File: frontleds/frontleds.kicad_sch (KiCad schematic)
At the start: 1 part, among them J1 Conn_01x02_MountingPin

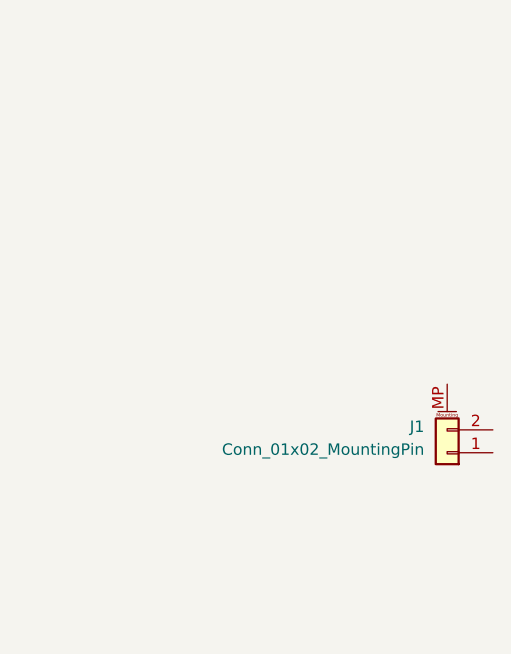
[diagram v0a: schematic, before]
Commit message: front led base layout done, should probably move resistors onto this board
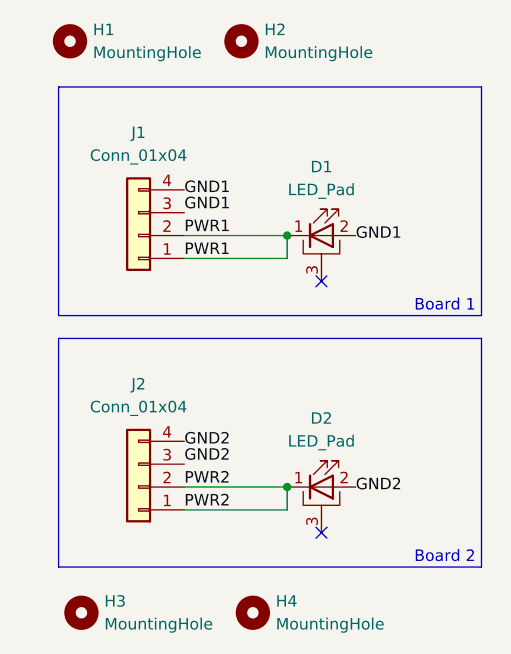
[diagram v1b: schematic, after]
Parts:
- removed J1: Conn_01x02_MountingPin, Connector_JST:JST_PH_B2B-PH-SM4-TB_1x02-1MP_P2.00mm_Vertical, symbol Connector_Generic_MountingPin:Conn_01x02_MountingPin
- added D1, D2: LED_Pad, LED_SMD:LED_Cree-XP-GWT, symbol Device:LED_Pad
- added H1, H2, H3, H4: MountingHole, MountingHole:MountingHole_2.7mm_M2.5_DIN965, symbol Mechanical:MountingHole
- added J1, J2: Conn_01x04, Connector_JST:JST_PH_B4B-PH-K_1x04_P2.00mm_Vertical, symbol Connector_Generic:Conn_01x04
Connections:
- new net GND1: D1.2 (A), J1.3 (Pin_3), J1.4 (Pin_4)
- new net GND2: D2.2 (A), J2.3 (Pin_3), J2.4 (Pin_4)
- new net PWR1: D1.1 (K), J1.1 (Pin_1), J1.2 (Pin_2)
- new net PWR2: D2.1 (K), J2.1 (Pin_1), J2.2 (Pin_2)
- no-connect marks 0 -> 2
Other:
- note added: "Board 1"
- note added: "Board 2"

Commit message: smol boi
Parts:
- removed D2: LED_Pad, LED_SMD:LED_Cree-XP-GWT, symbol Device:LED_Pad
- removed H1, H2, H3, H4: MountingHole, MountingHole:MountingHole_2.7mm_M2.5_DIN965, symbol Mechanical:MountingHole
- removed J1, J2: Conn_01x04, Connector_JST:JST_PH_B4B-PH-K_1x04_P2.00mm_Vertical, symbol Connector_Generic:Conn_01x04
- added J3: Conn_02x10_Odd_Even, Connector_Samtec_HSEC8:Samtec_HSEC8-110-X-X-DV_2x10_P0.8mm_Edge, symbol Connector_Generic:Conn_02x10_Odd_Even
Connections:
- net GND1 is gone; now on net PWR1: D1.2 (A)
- net PWR1: now also J3.10 (Pin_10), J3.12 (Pin_12), J3.14 (Pin_14), J3.16 (Pin_16), J3.18 (Pin_18), J3.2 (Pin_2), J3.20 (Pin_20), J3.4 (Pin_4), J3.6 (Pin_6), J3.8 (Pin_8); no longer D1.1 (K)
- new net GND: D1.1 (K), J3.1 (Pin_1), J3.11 (Pin_11), J3.13 (Pin_13), J3.15 (Pin_15), J3.17 (Pin_17), J3.19 (Pin_19), J3.3 (Pin_3), J3.5 (Pin_5), J3.7 (Pin_7), J3.9 (Pin_9)
- no-connect marks 2 -> 1
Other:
- note removed: "Board 1"
- note removed: "Board 2"
- moved on the sheet: D1

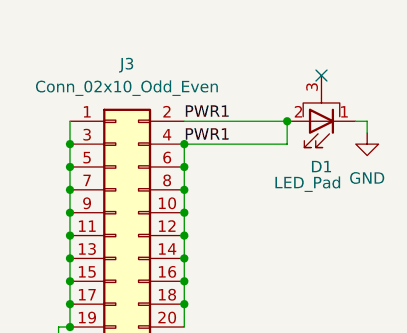
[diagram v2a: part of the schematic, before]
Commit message: changed front leds to use dedicated led current drivers
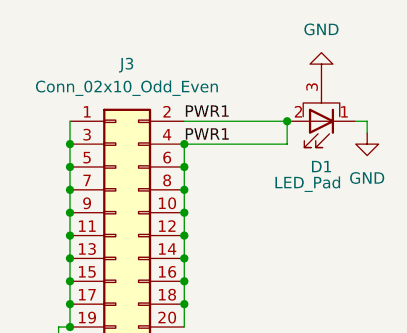
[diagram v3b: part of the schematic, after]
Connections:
- net GND: now also D1.3 (PAD)
- no-connect marks 1 -> 0
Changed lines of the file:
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@@
 		(color 0 0 0 0)
-	)
-	(no_connect
-		(at 69.85 54.61)
 	)
 	(wire
@@
 					(unit 1)
 				)
+			)
+		)
+	)
+	(symbol
+		(lib_id "power:GND")
+		(at 69.85 54.61 180)
+		(unit 1)
+		(exclude_from_sim no)
+		(in_bom yes)
+		(on_board yes)
+		(dnp no)
+		(fields_autoplaced yes)
+		(property "Reference" "#PWR03"
+			(at 69.85 48.26 0)
+			(effects
+				(font
+					(size 1.27 1.27)
+				)
+				(hide yes)
+			)
+		)
+		(property "Value" "GND"
+			(at 69.85 49.53 0)
+			(effects
+				(font
+					(size 1.27 1.27)
+				)
+			)
+		)
+		(property "Footprint" ""
+			(at 69.85 54.61 0)
+			(effects
+				(font
+					(size 1.27 1.27)
+				)
+				(hide yes)
+			)
+		)
+		(property "Datasheet" ""
+			(at 69.85 54.61 0)
+			(effects
+				(font
+					(size 1.27 1.27)
+				)
+				(hide yes)
+			)
+		)
+		(property "Description" "Power symbol creates a global label with name \"GND\" , ground"
+			(at 69.85 54.61 0)
+			(effects
+				(font
+					(size 1.27 1.27)
+				)
+				(hide yes)
+			)
+		)
+		(pin "1"
+		)
+		(instances
+			(project "frontleds"
+				(path "/ad2684eb-c2bb-4fca-b716-3281952c7862"
+					(reference "#PWR03")
+					(unit 1)
+				)

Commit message: small changes to leds
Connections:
- net PWR1 renamed PWR
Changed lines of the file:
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@@
-	)
-	(junction
-		(at 66.04 59.69)
-		(diameter 0)
-		(color 0 0 0 0)
 	)
 	(junction
@@
 	)
 	(junction
+		(at 54.61 59.69)
+		(diameter 0)
+		(color 0 0 0 0)
+	)
+	(junction
 		(at 54.61 77.47)
 		(diameter 0)
@@
 	)
 	(junction
+		(at 54.61 67.31)
+		(diameter 0)
+		(color 0 0 0 0)
+	)
+	(junction
+		(at 41.91 82.55)
+		(diameter 0)
+		(color 0 0 0 0)
+	)
+	(junction
 		(at 54.61 62.23)
 		(diameter 0)
@@
 	)
 	(junction
-		(at 54.61 67.31)
-		(diameter 0)
-		(color 0 0 0 0)
-	)
-	(junction
-		(at 41.91 82.55)
-		(diameter 0)
-		(color 0 0 0 0)
-	)
-	(junction
 		(at 41.91 77.47)
 		(diameter 0)
@@
 	(wire
 		(pts
+			(xy 54.61 59.69) (xy 54.61 62.23)
+		)
+		(stroke
+			(width 0)
+			(type default)
+		)
+	)
+	(wire
+		(pts
 			(xy 74.93 60.96) (xy 74.93 59.69)
 		)
@@
 	(wire
 		(pts
-			(xy 66.04 62.23) (xy 66.04 59.69)
-		)
-		(stroke
-			(width 0)
-			(type default)
-		)
-	)
-	(wire
-		(pts
 			(xy 41.91 77.47) (xy 41.91 80.01)
 		)
@@
 	(wire
 		(pts
-			(xy 54.61 62.23) (xy 66.04 62.23)
-		)
-		(stroke
-			(width 0)
-			(type default)
-		)
-	)
-	(wire
-		(pts
 			(xy 54.61 67.31) (xy 54.61 69.85)
 		)
@@
 		)
 	)
-	(label "PWR1"
+	(label "PWR"
 		(at 54.61 59.69 0)
 		(effects
 			(font
-				(size 1.27 1.27)
-			)
-			(justify left bottom)
-		)
-	)
-	(label "PWR1"
-		(at 54.61 62.23 0)
-		(effects
-			(font

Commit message: Production of leds and pcb
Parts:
- D1: LCSC (none) -> C17401863
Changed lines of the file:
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@@
+			)
+		)
+		(property "LCSC" "C17401863"
+			(at 69.85 59.69 0)
+			(effects
+				(font
+					(size 1.27 1.27)
+				)
+				(hide yes)
 			)
 		)

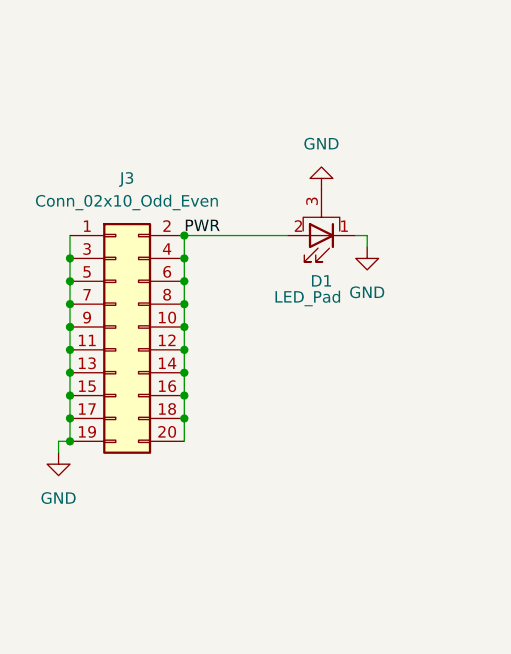
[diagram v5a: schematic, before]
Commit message: bro how does this work (fix led symbol footprint and model)
idk why frontleds can use drylettuce symbols but not footprints/3d models liek whaaaaa
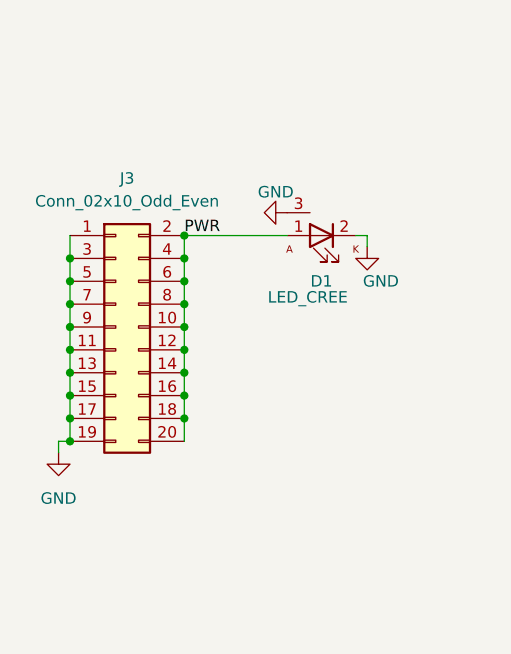
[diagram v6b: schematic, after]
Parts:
- D1: value LED_Pad -> LED_CREE; footprint LED_SMD:LED_Cree-XP-GWT -> Dry_Lettuce_LED:LED_Cree-XPGBWT; symbol Device:LED_Pad -> Dry_Lettuce:LED_CREE-XPGBWT
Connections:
- net GND: now also D1.2 (A); no longer D1.1 (K)
- net PWR: now also D1.1 (K); no longer D1.2 (A)
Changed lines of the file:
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@@
 (kicad_sch
-	(version 20250114)
+	(version 20260306)
 	(generator "eeschema")
-	(generator_version "9.0")
+	(generator_version "10.0")
 	(paper "A4")
 	(junction
@@
 		(at 46.99 69.85 0)
 		(unit 1)
+		(body_style 1)
 		(exclude_from_sim no)
 		(in_bom yes)
 		(on_board yes)
+		(in_pos_files yes)
 		(dnp no)
 		(fields_autoplaced yes)
 		(property "Reference" "J3"
 			(at 48.26 53.34 0)
+			(show_name no)
+			(do_not_autoplace no)
 			(effects
 				(font
@@
 		(property "Value" "Conn_02x10_Odd_Even"
 			(at 48.26 55.88 0)
+			(show_name no)
+			(do_not_autoplace no)
 			(effects
 				(font
@@
 		(property "Footprint" "Connector_Samtec_HSEC8:Samtec_HSEC8-110-X-X-DV_2x10_P0.8mm_Edge"
 			(at 46.99 69.85 0)
-			(effects
-				(font
-					(size 1.27 1.27)
-				)
-				(hide yes)
-			)
-		)
-		(property "Datasheet" "~"
+			(hide yes)
+			(show_name no)
+			(do_not_autoplace no)
+			(effects
+				(font
+					(size 1.27 1.27)
+				)
+			)
+		)
+		(property "Datasheet" ""
 			(at 46.99 69.85 0)
-			(effects
-				(font
-					(size 1.27 1.27)
-				)
-				(hide yes)
+			(hide yes)
+			(show_name no)
+			(do_not_autoplace no)
+			(effects
+				(font
+					(size 1.27 1.27)
+				)
 			)
 		)
 		(property "Description" "Generic connector, double row, 02x10, odd/even pin numbering scheme (row 1 odd numbers, row 2 even numbers), script generated (kicad-library-utils/schlib/autogen/connector/)"
 			(at 46.99 69.85 0)
-			(effects
-				(font
-					(size 1.27 1.27)
-				)
-				(hide yes)
+			(hide yes)
+			(show_name no)
+			(do_not_autoplace no)
+			(effects
+				(font
+					(size 1.27 1.27)
+				)
 			)
 		)
@@
 		)
 		(instances
-			(project ""
+			(project "frontleds"
 				(path "/ad2684eb-c2bb-4fca-b716-3281952c7862"
 					(reference "J3")
@@
 	(symbol
 		(lib_id "power:GND")
-		(at 69.85 54.61 180)
+		(at 66.04 57.15 270)
 		(unit 1)
+		(body_style 1)
 		(exclude_from_sim no)
 		(in_bom yes)
 		(on_board yes)
+		(in_pos_files yes)
 		(dnp no)
-		(fields_autoplaced yes)
 		(property "Reference" "#PWR03"
-			(at 69.85 48.26 0)
-			(effects
-				(font
-					(size 1.27 1.27)
-				)
-				(hide yes)
+			(at 59.69 57.15 0)
+			(hide yes)
+			(show_name no)
+			(do_not_autoplace no)
+			(effects
+				(font
+					(size 1.27 1.27)
+				)
 			)
 		)
 		(property "Value" "GND"
-			(at 69.85 49.53 0)
+			(at 64.77 54.864 90)
+			(show_name no)
+			(do_not_autoplace no)
 			(effects
 				(font
@@
 		)
 		(property "Footprint" ""
-			(at 69.85 54.61 0)
-			(effects
-				(font
-					(size 1.27 1.27)
-				)
-				(hide yes)
+			(at 66.04 57.15 0)
+			(hide yes)
+			(show_name no)
+			(do_not_autoplace no)
+			(effects
+				(font
+					(size 1.27 1.27)
+				)
 			)
 		)
 		(property "Datasheet" ""
-			(at 69.85 54.61 0)
-			(effects
-				(font
-					(size 1.27 1.27)
-				)
-				(hide yes)
+			(at 66.04 57.15 0)
+			(hide yes)
+			(show_name no)
+			(do_not_autoplace no)
+			(effects
+				(font
+					(size 1.27 1.27)
+				)
 			)
 		)
 		(property "Description" "Power symbol creates a global label with name \"GND\" , ground"
-			(at 69.85 54.61 0)
-			(effects
-				(font
-					(size 1.27 1.27)
-				)
-				(hide yes)
+			(at 66.04 57.15 0)
+			(hide yes)
+			(show_name no)
+			(do_not_autoplace no)
+			(effects
+				(font
+					(size 1.27 1.27)
+				)
 			)
 		)
@@
 	)
 	(symbol
-		(lib_id "Device:LED_Pad")
+		(lib_id "Dry_Lettuce:LED_CREE-XPGBWT")
 		(at 69.85 59.69 180)
 		(unit 1)
+		(body_style 1)
 		(exclude_from_sim no)
 		(in_bom yes)
 		(on_board yes)
+		(in_pos_files yes)
 		(dnp no)
 		(property "Reference" "D1"
 			(at 69.85 64.77 0)
-			(effects
-				(font
-					(size 1.27 1.27)
-				)
-			)
-		)
-		(property "Value" "LED_Pad"
+			(show_name no)
+			(do_not_autoplace no)
+			(effects
+				(font
+					(size 1.27 1.27)
+				)
+			)
+		)
+		(property "Value" "LED_CREE"
 			(at 68.326 66.548 0)
-			(effects
-				(font
-					(size 1.27 1.27)
-				)
-			)
-		)
-		(property "Footprint" "LED_SMD:LED_Cree-XP-GWT"
+			(show_name no)
+			(do_not_autoplace no)
+			(effects
+				(font
+					(size 1.27 1.27)
+				)
+			)
+		)
+		(property "Footprint" "Dry_Lettuce_LED:LED_Cree-XPGBWT"
 			(at 69.85 59.69 0)
-			(effects
-				(font
-					(size 1.27 1.27)
-				)
-				(hide yes)
-			)
-		)
-		(property "Datasheet" "~"
+			(hide yes)
+			(show_name no)
+			(do_not_autoplace no)
+			(effects
+				(font
+					(size 1.27 1.27)
+				)
+			)
+		)
+		(property "Datasheet" ""
 			(at 69.85 59.69 0)
-			(effects
-				(font
-					(size 1.27 1.27)
-				)
-				(hide yes)
+			(hide yes)
+			(show_name no)
+			(do_not_autoplace no)
+			(effects
+				(font
+					(size 1.27 1.27)
+				)
 			)
 		)
 		(property "Description" "Light emitting diode with pad"
-			(at 69.85 59.69 0)
-			(effects
-				(font
-					(size 1.27 1.27)
-				)
-				(hide yes)
+			(at 70.358 52.07 0)
+			(hide yes)
+			(show_name no)
+			(do_not_autoplace no)
+			(effects
+				(font
+					(size 1.27 1.27)
+				)
 			)
 		)
 		(property "LCSC" "C17401863"
 			(at 69.85 59.69 0)
-			(effects
-				(font
-					(size 1.27 1.27)
-				)
-				(hide yes)
+			(hide yes)
+			(show_name no)
+			(do_not_autoplace no)
+			(effects
+				(font
+					(size 1.27 1.27)
+				)
 			)
 		)
@@
 		)
 		(instances
-			(project ""
+			(project "frontleds"
 				(path "/ad2684eb-c2bb-4fca-b716-3281952c7862"
 					(reference "D1")
@@
 		(at 40.64 83.82 0)
 		(unit 1)
+		(body_style 1)
 		(exclude_from_sim no)
 		(in_bom yes)
 		(on_board yes)
+		(in_pos_files yes)
 		(dnp no)
 		(fields_autoplaced yes)
 		(property "Reference" "#PWR02"
 			(at 40.64 90.17 0)
-			(effects
-				(font
-					(size 1.27 1.27)
-				)
-				(hide yes)
+			(hide yes)
+			(show_name no)
+			(do_not_autoplace no)
+			(effects
+				(font
+					(size 1.27 1.27)
+				)
 			)
 		)
 		(property "Value" "GND"
 			(at 40.64 88.9 0)
+			(show_name no)
+			(do_not_autoplace no)
 			(effects
 				(font
@@
 		(property "Footprint" ""
 			(at 40.64 83.82 0)
-			(effects
-				(font
-					(size 1.27 1.27)
-				)
-				(hide yes)
+			(hide yes)
+			(show_name no)
+			(do_not_autoplace no)
+			(effects
+				(font
+					(size 1.27 1.27)
+				)
 			)
 		)
 		(property "Datasheet" ""
 			(at 40.64 83.82 0)
-			(effects
-				(font
-					(size 1.27 1.27)
-				)
-				(hide yes)
+			(hide yes)
+			(show_name no)
+			(do_not_autoplace no)
+			(effects
+				(font
+					(size 1.27 1.27)
+				)
 			)
 		)
 		(property "Description" "Power symbol creates a global label with name \"GND\" , ground"
 			(at 40.64 83.82 0)
-			(effects
-				(font
-					(size 1.27 1.27)
-				)
-				(hide yes)
+			(hide yes)
+			(show_name no)
+			(do_not_autoplace no)
+			(effects
+				(font
+					(size 1.27 1.27)
+				)
 			)
 		)
@@
 		(at 74.93 60.96 0)
 		(unit 1)
+		(body_style 1)
 		(exclude_from_sim no)
 		(in_bom yes)
 		(on_board yes)
+		(in_pos_files yes)
 		(dnp no)
-		(fields_autoplaced yes)
 		(property "Reference" "#PWR01"
 			(at 74.93 67.31 0)
-			(effects
-				(font
-					(size 1.27 1.27)
-				)
-				(hide yes)
+			(hide yes)
+			(show_name no)
+			(do_not_autoplace no)
+			(effects
+				(font
+					(size 1.27 1.27)
+				)
 			)
 		)
 		(property "Value" "GND"
-			(at 74.93 66.04 0)
+			(at 76.454 64.77 0)
+			(show_name no)
+			(do_not_autoplace no)
 			(effects
 				(font
@@
 		(property "Footprint" ""
 			(at 74.93 60.96 0)
-			(effects
-				(font
-					(size 1.27 1.27)
-				)
-				(hide yes)
+			(hide yes)
+			(show_name no)
+			(do_not_autoplace no)
+			(effects
+				(font
+					(size 1.27 1.27)
+				)
 			)
 		)
 		(property "Datasheet" ""
 			(at 74.93 60.96 0)
-			(effects
-				(font
-					(size 1.27 1.27)
-				)
-				(hide yes)
+			(hide yes)
+			(show_name no)
+			(do_not_autoplace no)
+			(effects
+				(font
+					(size 1.27 1.27)
+				)
 			)
 		)
 		(property "Description" "Power symbol creates a global label with name \"GND\" , ground"
 			(at 74.93 60.96 0)
-			(effects
-				(font
-					(size 1.27 1.27)
-				)
-				(hide yes)
+			(hide yes)
+			(show_name no)
+			(do_not_autoplace no)
+			(effects
+				(font
+					(size 1.27 1.27)
+				)
 			)
 		)
@@
 		)
 		(instances
-			(project ""
+			(project "frontleds"
 				(path "/ad2684eb-c2bb-4fca-b716-3281952c7862"
 					(reference "#PWR01")
